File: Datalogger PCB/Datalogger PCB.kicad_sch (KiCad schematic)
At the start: 44 parts, among them J1 Conn_01x02_Pin, M1 Motor_Servo, M2 Motor_Servo, M3 Motor_Servo, M4 Motor_Servo, U1 Teensy4.1, U2 BNO055, U3 LPS25HB, U4 AMS1117-5.0, U5 NRF24L01_Breakout, U6 VN5E160STR-E, U7 VN5E160STR-E, U8 VN5E160STR-E, U9 VN5E160STR-E

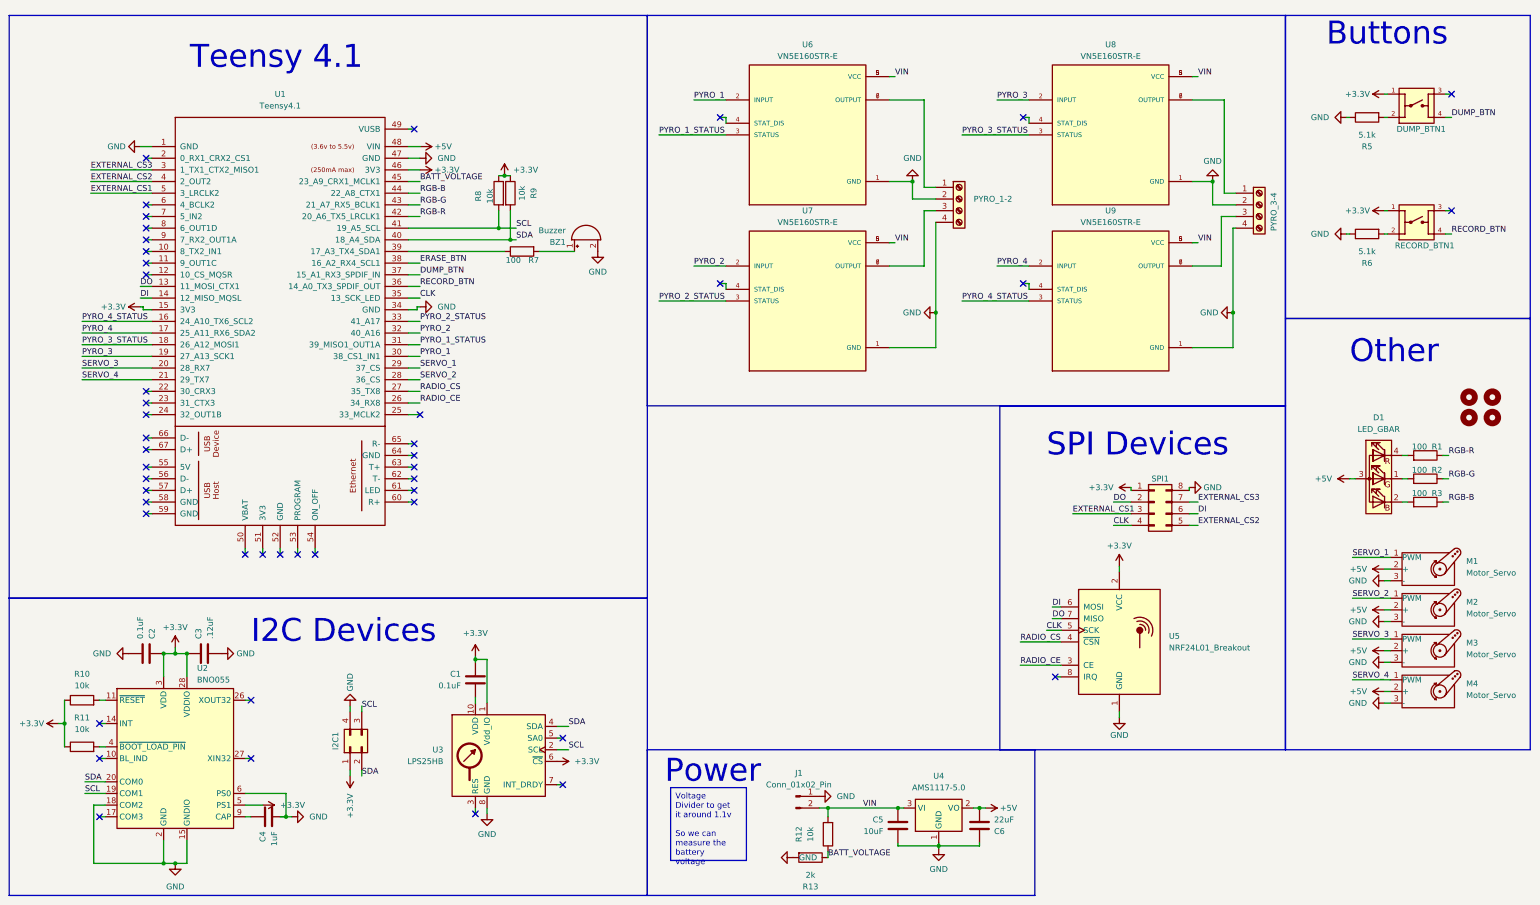
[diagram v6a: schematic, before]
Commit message: Added screw terminal for switching on/off pyro channels
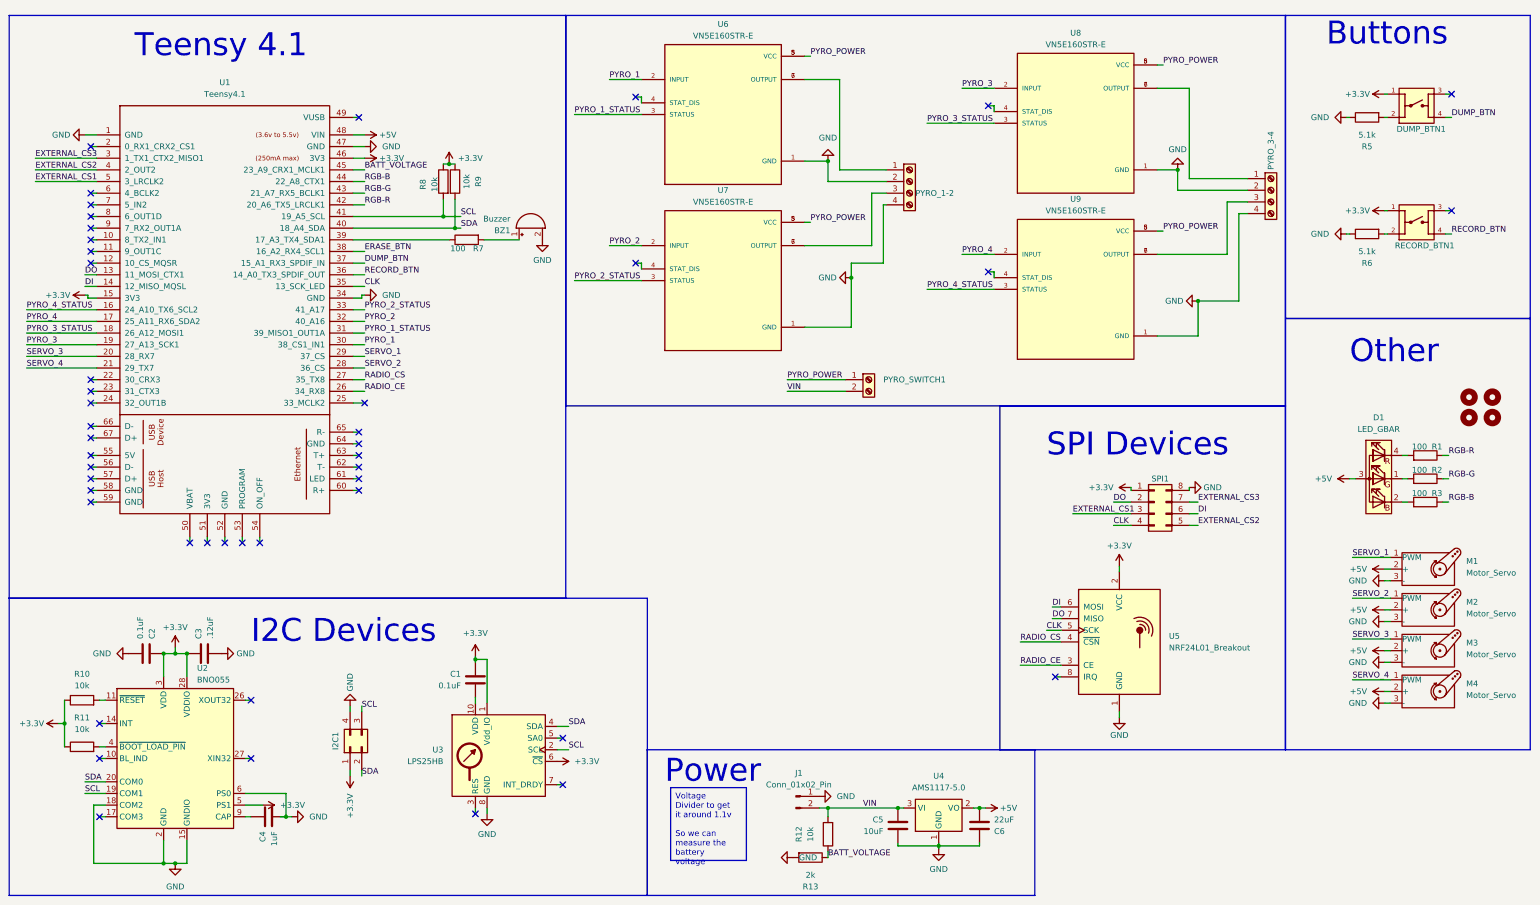
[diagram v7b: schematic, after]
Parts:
- added PYRO_SWITCH1: Screw_Terminal_01x02, TerminalBlock:TerminalBlock_bornier-2_P5.08mm, symbol Connector:Screw_Terminal_01x02
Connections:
- net VIN: now also PYRO_SWITCH1.2 (Pin_2); no longer U6.5 (VCC), U6.8 (VCC), U7.5 (VCC), U7.8 (VCC), U8.5 (VCC), U8.8 (VCC), U9.5 (VCC), U9.8 (VCC)
- new net PYRO_POWER: PYRO_SWITCH1.1 (Pin_1), U6.5 (VCC), U6.8 (VCC), U7.5 (VCC), U7.8 (VCC), U8.5 (VCC), U8.8 (VCC), U9.5 (VCC), U9.8 (VCC)
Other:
- moved on the sheet: BZ1, PYRO_1-2, PYRO_3-4, R7, R8, R9, U1, U6, U7, U8, U9

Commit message: Fixed Decoupling Cap for Barometer
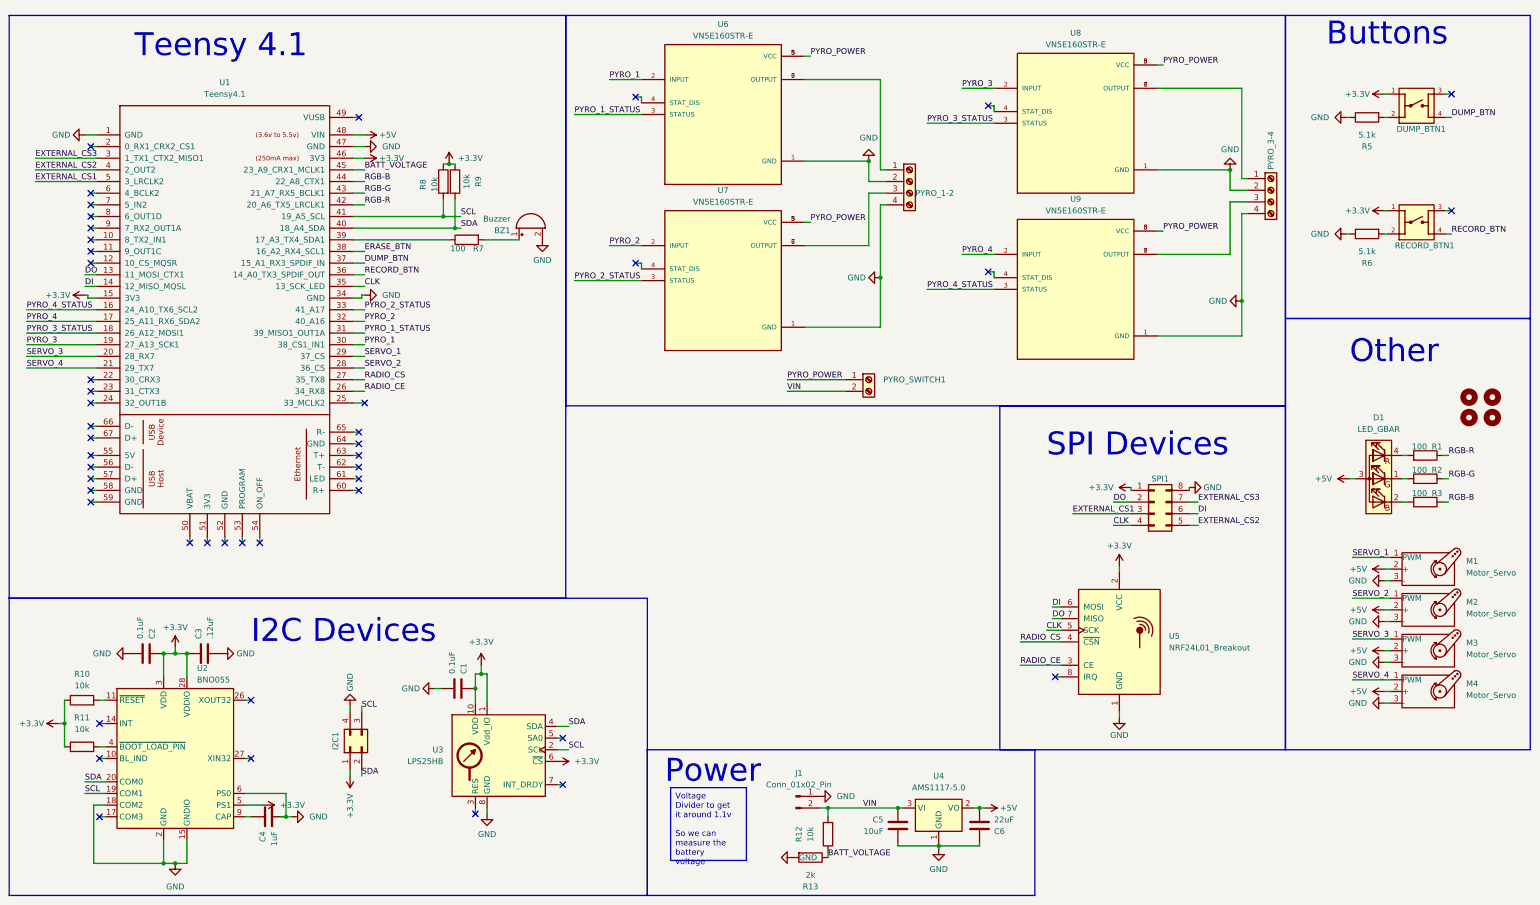
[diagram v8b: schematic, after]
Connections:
- net +3.3V: now also U3.10 (VDD)
- net GND: now also C1.2
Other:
- moved on the sheet: C1
